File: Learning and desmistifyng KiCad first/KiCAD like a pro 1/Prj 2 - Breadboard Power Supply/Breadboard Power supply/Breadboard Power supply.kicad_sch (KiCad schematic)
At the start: 7 parts, among them J1 Barrel_Jack_Switch, J2 Screw_Terminal_01x02, J3 Screw_Terminal_01x02

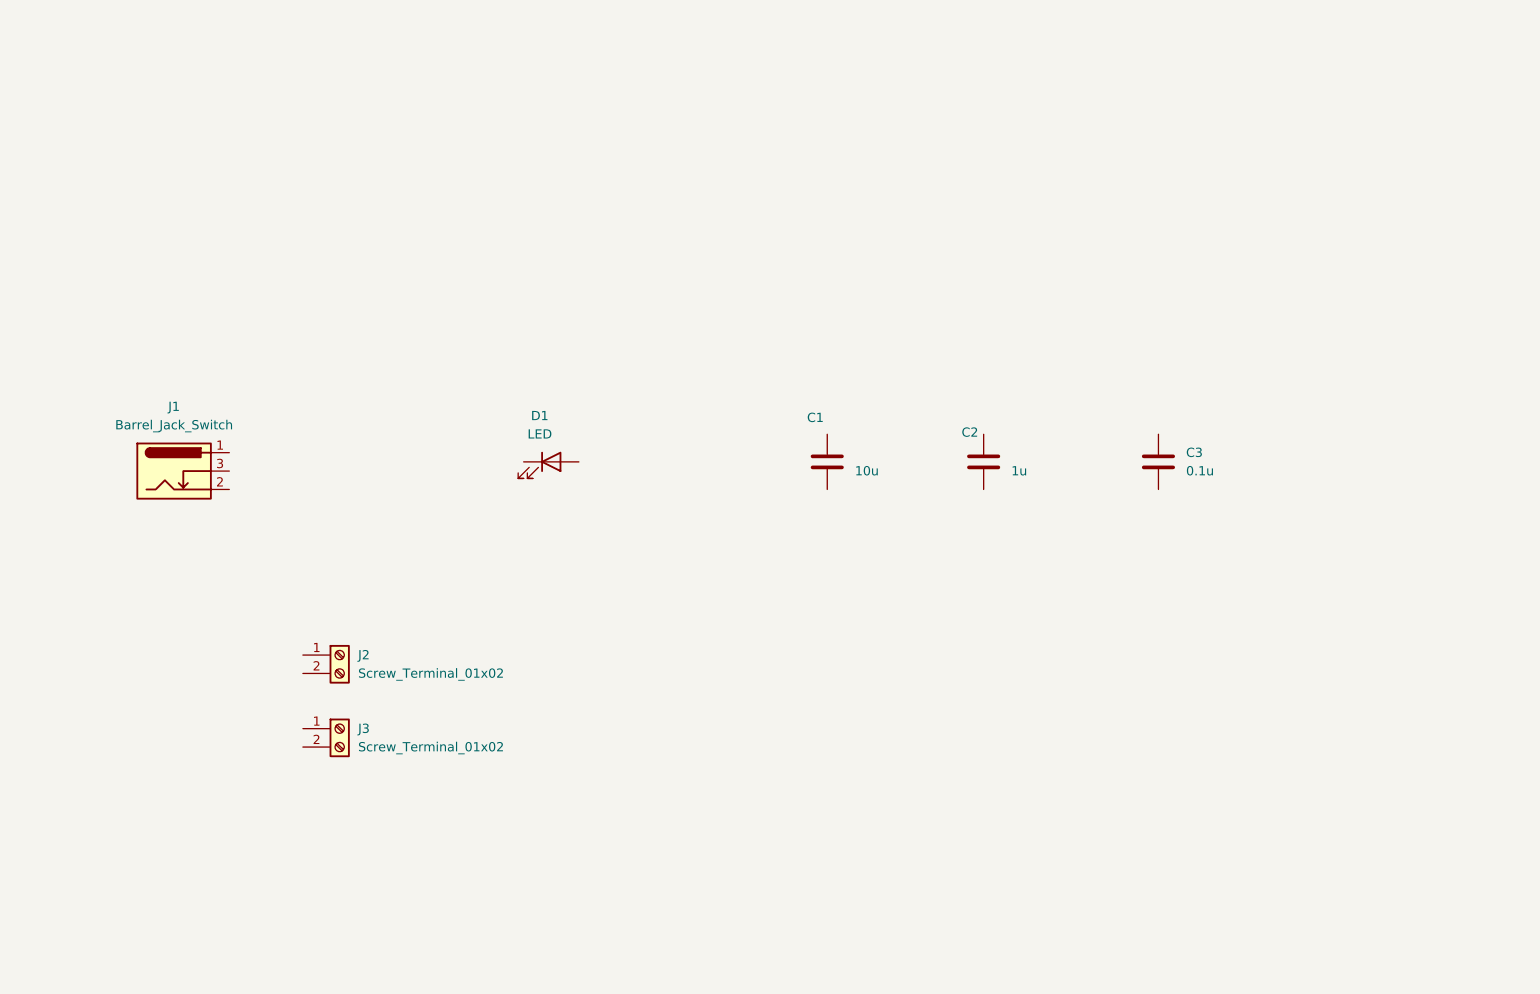
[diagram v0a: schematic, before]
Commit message: update the schematic for the breadboard power supply
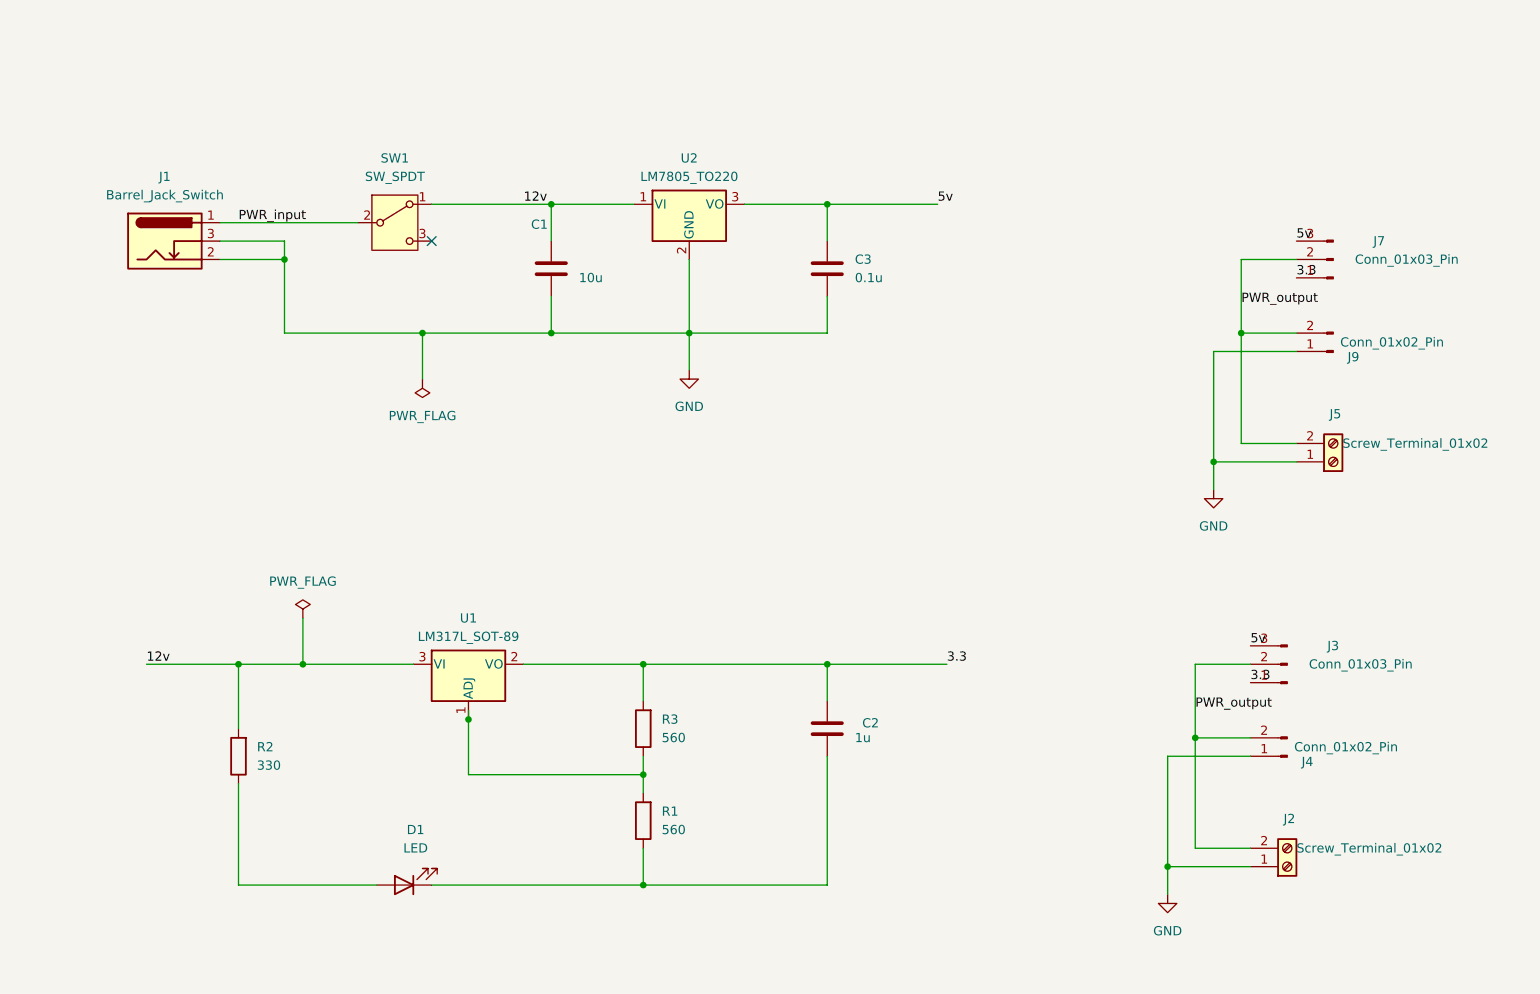
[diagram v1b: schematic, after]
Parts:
- removed J3: Screw_Terminal_01x02, symbol Connector:Screw_Terminal_01x02
- added J3, J7: Conn_01x03_Pin, Connector_PinHeader_2.54mm:PinHeader_1x02_P2.54mm_Vertical, symbol Connector:Conn_01x03_Pin
- added J4, J9: Conn_01x02_Pin, Connector_PinHeader_2.54mm:PinHeader_1x02_P2.54mm_Vertical, symbol Connector:Conn_01x02_Pin
- added J5: Screw_Terminal_01x02, TerminalBlock:TerminalBlock_bornier-2_P5.08mm, symbol Connector:Screw_Terminal_01x02
- added R1, R3: 560, Resistor_THT:R_Axial_DIN0204_L3.6mm_D1.6mm_P7.62mm_Horizontal, symbol Device:R
- added R2: 330, Resistor_THT:R_Axial_DIN0204_L3.6mm_D1.6mm_P7.62mm_Horizontal, symbol Device:R
- added SW1: SW_SPDT, Button_Switch_THT:SW_TH_Tactile_Omron_B3F-110x, symbol Switch:SW_SPDT
- added U1: LM317L_SOT-89, Package_TO_SOT_SMD:SOT-89-3, symbol Regulator_Linear:LM317L_SOT-89
- added U2: LM7805_TO220, Package_TO_SOT_THT:TO-220-3_Vertical, symbol Regulator_Linear:LM7805_TO220
- C2, C3: footprint (none) -> Capacitor_THT:C_Disc_D3.0mm_W1.6mm_P2.50mm
- D1: footprint (none) -> LED_THT:LED_D5.0mm
- J1: footprint (none) -> Connector_BarrelJack:BarrelJack_Horizontal
- J2: footprint (none) -> TerminalBlock:TerminalBlock_bornier-2_P5.08mm
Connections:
- net at C3.1: no longer names the net of C3.1
- net at C3.1: now also J3.3 (Pin_3), J7.3 (Pin_3), U2.3 (VO)
- net GND: now reaches C3.2
- net GND: now also C1.2, J1.2, J1.3, J2.1 (Pin_1), J4.1 (Pin_1), J5.1 (Pin_1), J9.1 (Pin_1), U2.2 (GND)
- net at D1.1 (K): now also C2.2, R1.1
- net at D1.2 (A): now also R2.1
- net PWR_input: now reaches J1.1
- net PWR_input: now also SW1.2 (B)
- net 12v: now reaches C1.1
- net 12v: now also R2.2, SW1.1 (A), U1.3 (VI), U2.1 (VI)
- net PWR_output: now reaches J2.2 (Pin_2)
- net PWR_output: now also J3.2 (Pin_2), J4.2 (Pin_2), J5.2 (Pin_2), J7.2 (Pin_2), J9.2 (Pin_2)
- net 3.3: now reaches C2.1
- net 3.3: now also J3.1 (Pin_1), J7.1 (Pin_1), R3.2, U1.2 (VO)
- new net: R1.2, R3.1, U1.1 (ADJ)
- no-connect marks 0 -> 1
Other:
- moved on the sheet: C1, C2, C3, D1, J1

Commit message: update libraries and The breadboard power supply
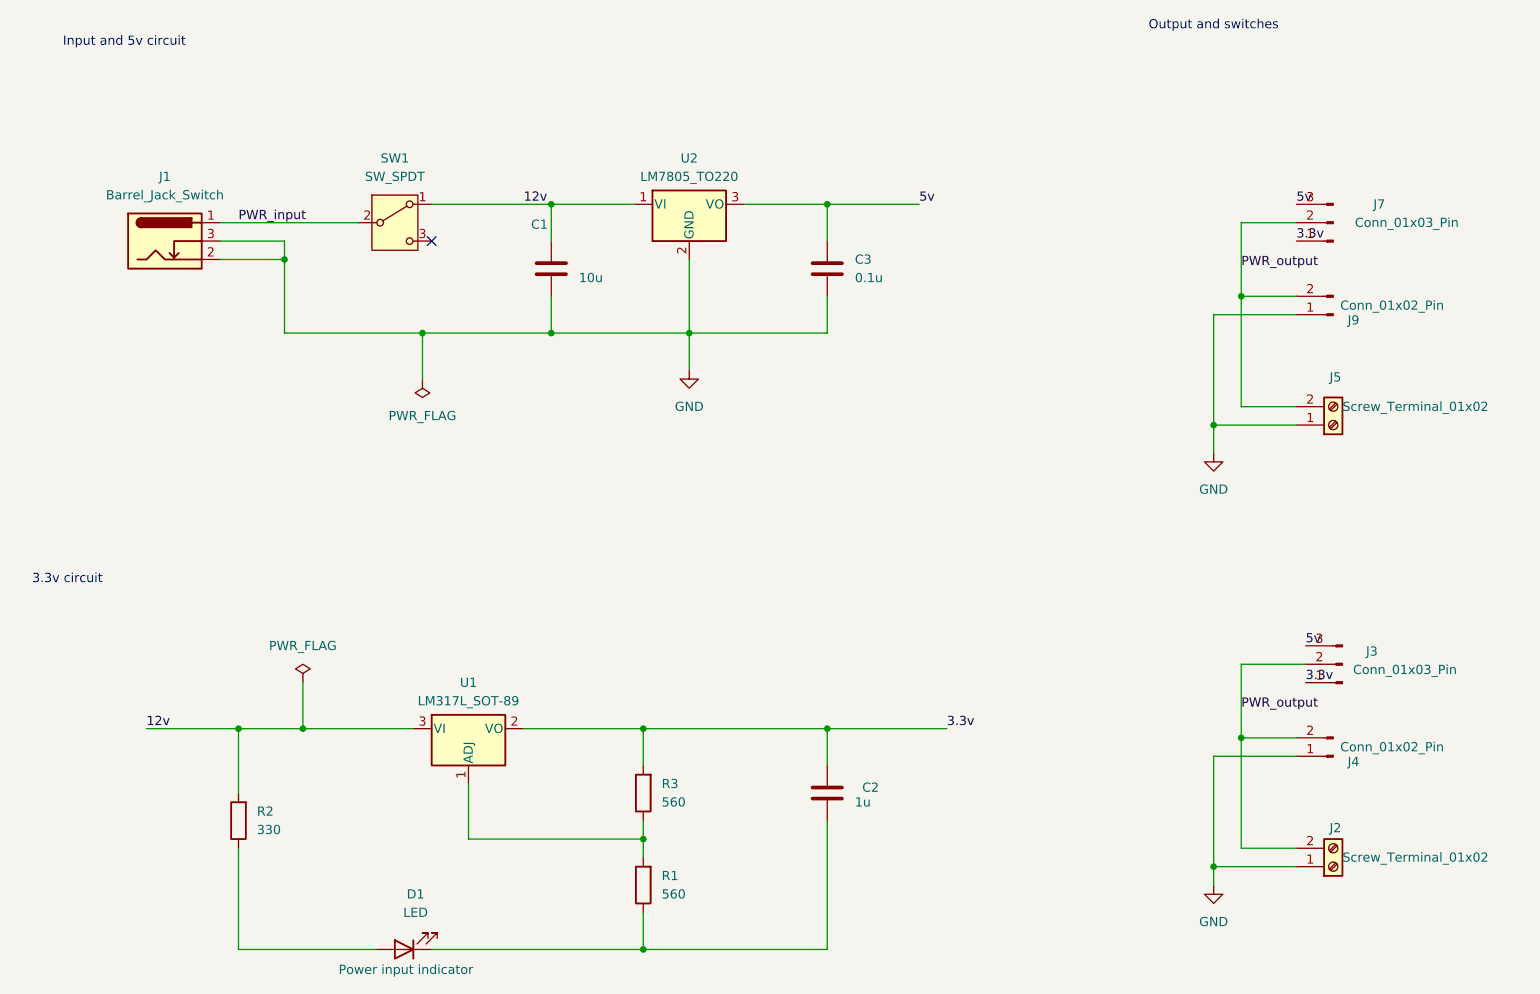
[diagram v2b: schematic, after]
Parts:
- D1: Purpose (none) -> Power input indicator
- J3, J7: footprint Connector_PinHeader_2.54mm:PinHeader_1x02_P2.54mm_Vertical -> Connector_PinHeader_2.54mm:PinHeader_1x03_P2.54mm_Vertical
- SW1: footprint Button_Switch_THT:SW_TH_Tactile_Omron_B3F-110x -> Button_Switch_THT:SW_Slide-03_Wuerth-WS-SLTV_10x2.5x6.4_P2.54mm
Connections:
- net 5v: now reaches C3.1, J3.3 (Pin_3), J7.3 (Pin_3), U2.3 (VO)
- net 3.3 renamed 3.3v
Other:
- note added: "3.3v circuit"
- note added: "Input and 5v circuit"
- note added: "Output and switches"
- moved on the sheet: C2, D1, J2, J4, J5, J7, J9, R1, R2, R3

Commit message: update breadboard power supply project
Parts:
- J3, J7: value Conn_01x03_Pin -> Conn_01x03_Male
- J4: value Conn_01x02_Pin -> Conn_01x02_Male
- J6: renamed from J9; value Conn_01x02_Pin -> Conn_01x02_Male
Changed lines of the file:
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@@
 			)
 		)
-		(property "Value" "Conn_01x02_Pin"
+		(property "Value" "Conn_01x02_Male"
 			(at 225.298 119.38 0)
 			(effects
@@
 			)
 		)
-		(property "Value" "Conn_01x03_Pin"
+		(property "Value" "Conn_01x03_Male"
 			(at 227.076 108.712 0)
 			(effects
@@
 		(on_board yes)
 		(dnp no)
-		(property "Reference" "J9"
+		(property "Reference" "J6"
 			(at 219.964 60.452 0)
 			(effects
@@
 			)
 		)
-		(property "Value" "Conn_01x02_Pin"
+		(property "Value" "Conn_01x02_Male"
 			(at 225.298 58.42 0)
 			(effects
@@
 			(project "Breadboard Power supply"
 				(path "/7da24ccf-657a-48c6-ab85-8efcd1e74a3c"
-					(reference "J9")
+					(reference "J6")
 					(unit 1)
 				)
@@
 			)
 		)
-		(property "Value" "Conn_01x03_Pin"
+		(property "Value" "Conn_01x03_Male"
 			(at 227.33 46.99 0)
 			(effects
